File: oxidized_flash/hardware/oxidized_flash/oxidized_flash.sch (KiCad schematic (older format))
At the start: 37 parts, among them J1 USB_A, J2 Conn_ARM_JTAG_SWD_10, U1 LM1117-3.3, U2 ATSAMD51G18A-MU, U3 IS21ES

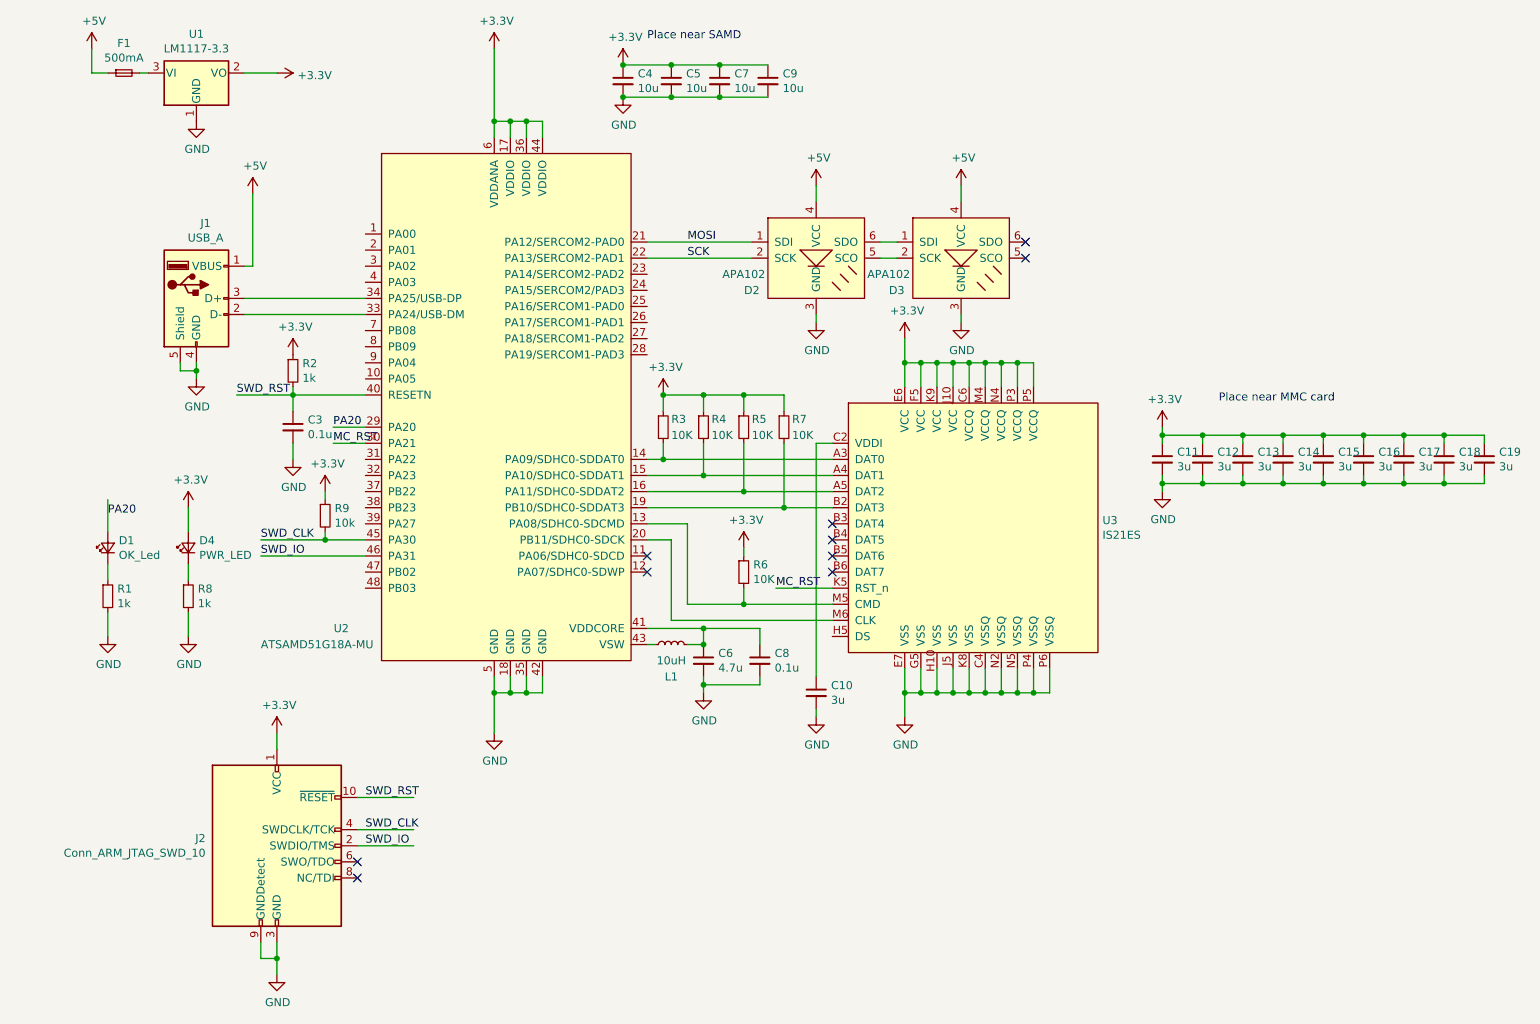
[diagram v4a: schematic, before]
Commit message: Rip out all the emmc stuff, just a samd with lights
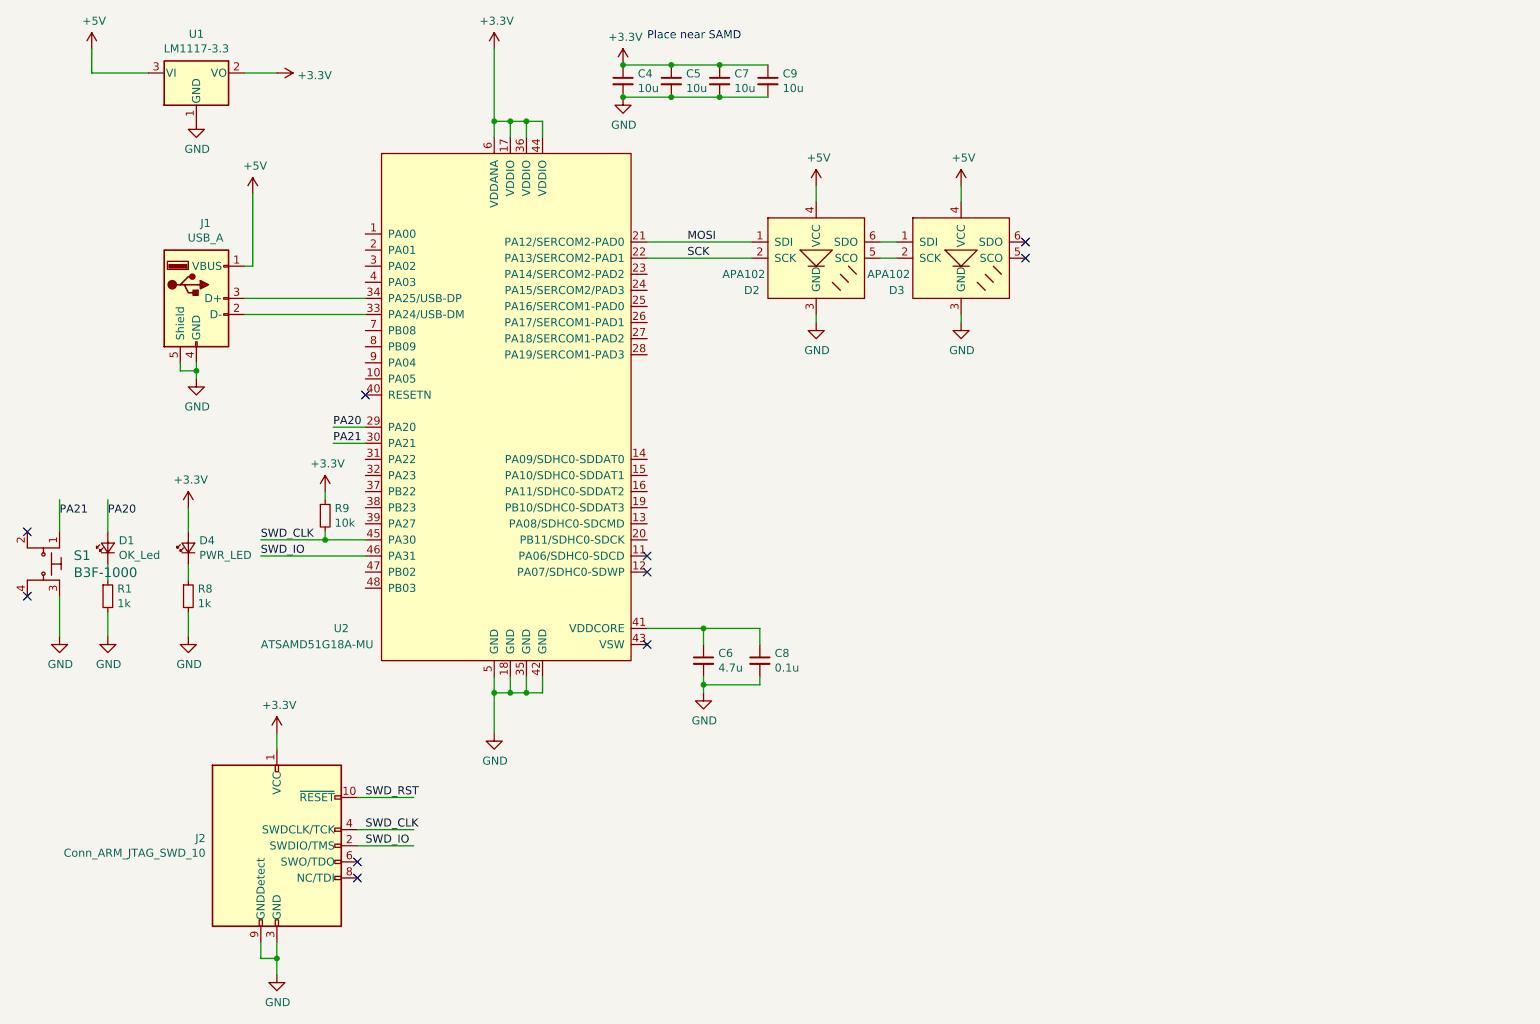
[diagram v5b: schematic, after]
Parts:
- removed C10, C11: 3u, Capacitor_SMD:C_0603_1608Metric, symbol Device:C_Small
- removed C12, C13, C14, C15, C16, C17, C18, C19: 3u, Capacitor_SMD:C_0603_1608Metric_Pad1.05x0.95mm_HandSolder, symbol Device:C_Small
- removed C3: 0.1u, Capacitor_SMD:C_0603_1608Metric, symbol Device:C_Small
- removed F1: 500mA, Fuse:Fuse_0603_1608Metric, symbol Device:Fuse_Small
- removed L1: 10uH, Inductor_SMD:L_0603_1608Metric, symbol Device:L_Small
- removed R2: 1k, Resistor_SMD:R_0603_1608Metric, symbol Device:R_Small
- removed R3, R4, R5: 10K, Resistor_SMD:R_0603_1608Metric, symbol Device:R_Small
- removed R6, R7: 10K, Resistor_SMD:R_0603_1608Metric_Pad1.05x0.95mm_HandSolder, symbol Device:R_Small
- removed U3: IS21ES, Custom_BGA:FBGA-153_14x14_11.5x13.0mm, symbol oxidized_flash-rescue:IS21ES-eMMC
- added S1: B3F-1000, Buttons_Switches_THT:SW_TH_Tactile_Omron_B3F-10xx, symbol dk_Tactile-Switches:B3F-1000
- C4, C5, C6, C7, C8, C9: footprint Capacitor_SMD:C_0603_1608Metric -> Capacitors_SMD:C_0603
- D1, D4: footprint LED_SMD:LED_0603_1608Metric -> LEDs:LED_0603
- J2: footprint Connector_PinHeader_1.27mm:PinHeader_2x05_P1.27mm_Vertical_SMD -> Pin_Headers:Pin_Header_Straight_2x05_Pitch1.27mm_SMD
- R1: footprint Resistor_SMD:R_0603_1608Metric -> Resistors_SMD:R_0603
- R8, R9: footprint Resistor_SMD:R_0603_1608Metric_Pad1.05x0.95mm_HandSolder -> Resistors_SMD:R_0603
- U1: footprint Package_TO_SOT_SMD:SOT-223 -> TO_SOT_Packages_SMD:SOT-223
- U2: footprint Package_DFN_QFN:QFN-48-1EP_7x7mm_P0.5mm_EP5.3x5.3mm -> Housings_DFN_QFN:QFN-48-1EP_7x7mm_Pitch0.5mm
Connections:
- net labels added: PA21
- net labels removed: MC_RST
- wire segments 184 -> 72
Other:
- note removed: "Place near MMC card"

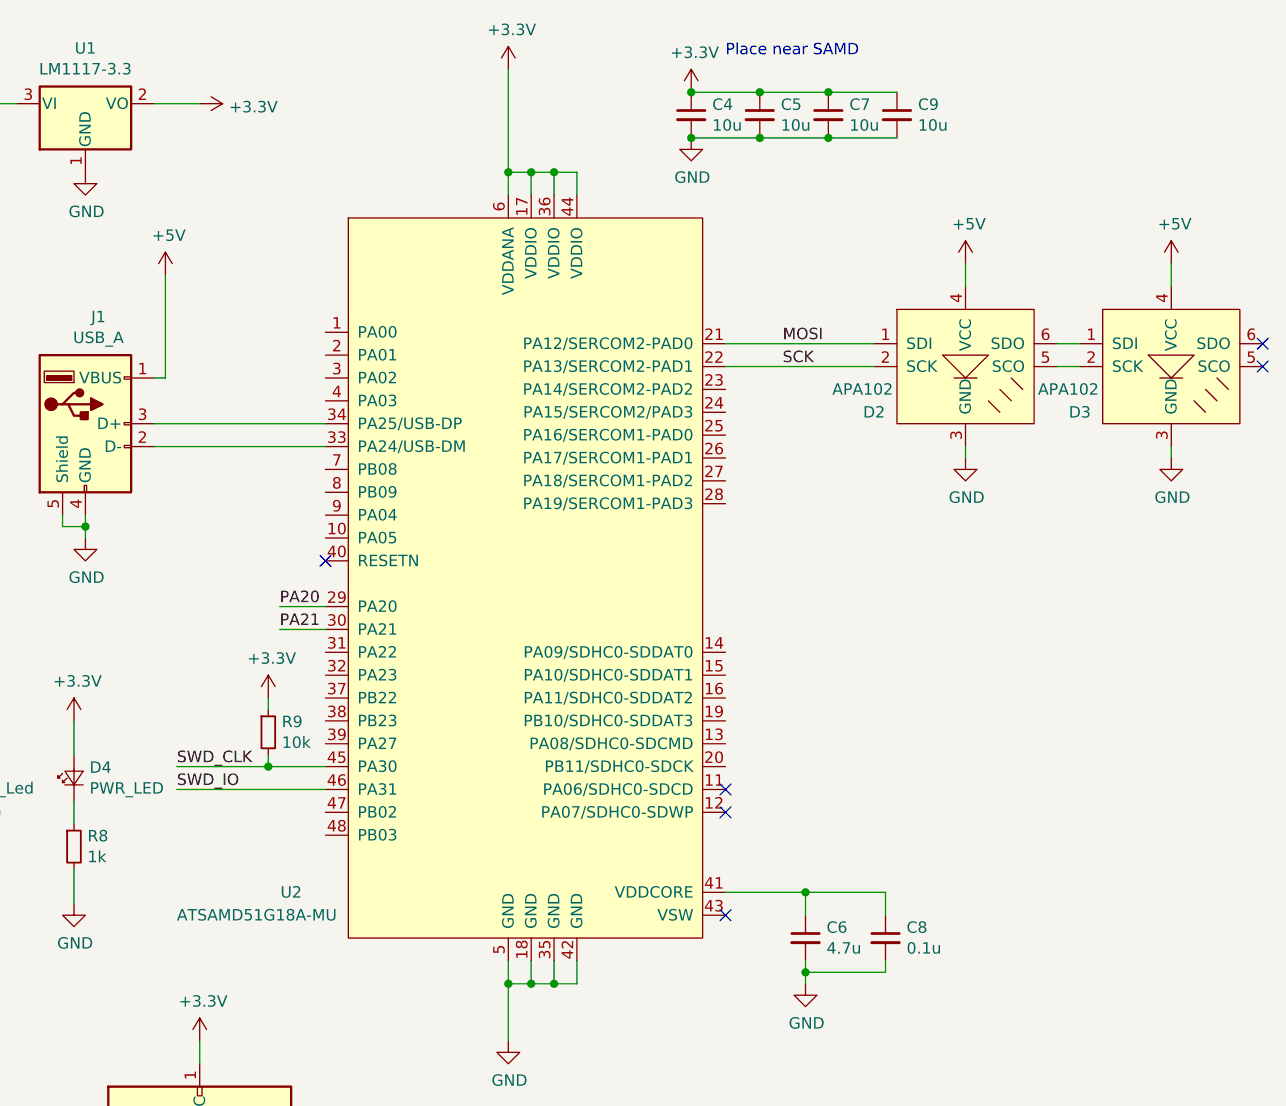
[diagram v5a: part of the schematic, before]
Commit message: Add 512M SPI flash
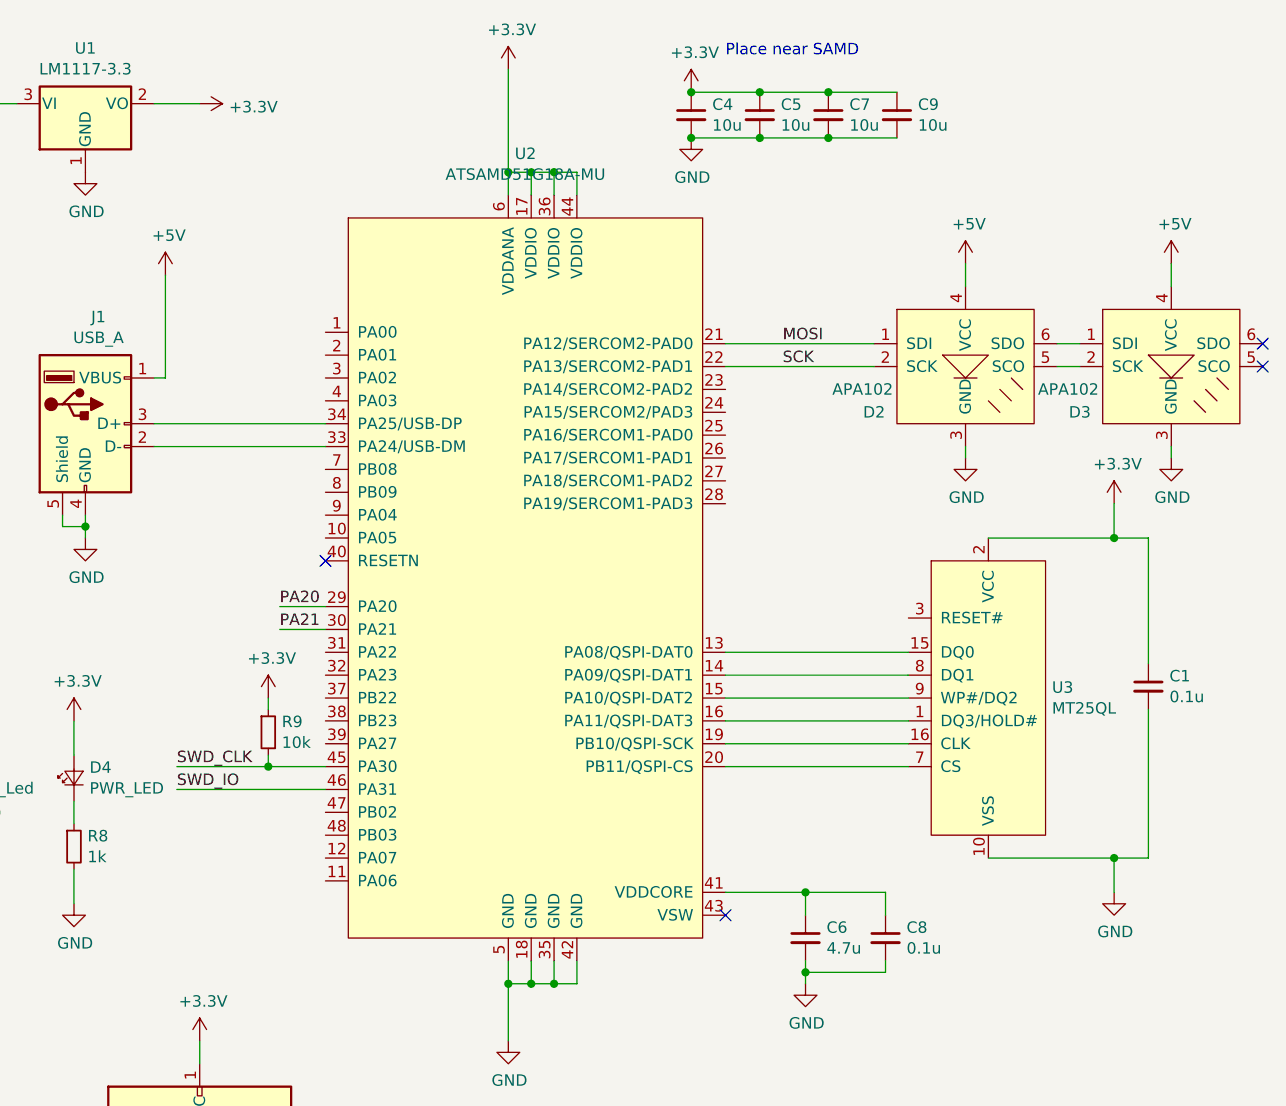
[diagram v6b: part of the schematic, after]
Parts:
- removed U2: ATSAMD51G18A-MU, Housings_DFN_QFN:QFN-48-1EP_7x7mm_Pitch0.5mm, symbol oxidized_flash-rescue:ATSAMD51G18A-MU-ATSAMD
- added C1: 0.1u, Capacitors_SMD:C_0603, symbol Device:C_Small
- added U2: ATSAMD51G18A-MU, Housings_DFN_QFN:QFN-48-1EP_7x7mm_Pitch0.5mm, symbol ATSAMD:ATSAMD51G18A-MU
- added U3: MT25QL, Housings_SSOP:SOP-16_4.4x10.4mm_Pitch1.27mm, symbol custom_ic:MT25QL
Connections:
- wire segments 72 -> 86
- no-connect marks 10 -> 8
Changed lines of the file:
@@
 	1    0    0    -1
 $EndComp
-NoConn ~ 4400 4200
-NoConn ~ 4400 4300
 Wire Wire Line
 	3450 4950 3450 5050
@@
 Wire Wire Line
 	3450 1600 3450 1500
-Wire Wire Line
-	1900 2600 2650 2600
-Wire Wire Line
-	1900 2700 2650 2700
 Wire Wire Line
 	3550 1600 3550 1500
@@
 PA20
 Wire Wire Line
-	2450 3400 2650 3400
-Wire Wire Line
 	1900 1200 2100 1200
 Wire Wire Line
@@
 Connection ~ 2400 4100
 Wire Wire Line
-	2400 4100 2650 4100
-Wire Wire Line
 	2400 3850 2400 3800
 $Comp
@@
 	1    0    0    -1
 $EndComp
-Wire Wire Line
-	2650 4200 2000 4200
 Text Label 2000 4200 0    50   ~ 0
 SWD_IO
@@
 Text Label 2450 3500 0    50   ~ 0
 PA21
-Wire Wire Line
-	2650 3500 2450 3500
 Wire Wire Line
 	750  3850 750  4050
@@
 Wire Wire Line
 	3450 5050 3450 5300
-$Comp
-L oxidized_flash-rescue:ATSAMD51G18A-MU-ATSAMD U2
-U 1 1 5C4804F6
+NoConn ~ 2650 3200
+$Comp
+L ATSAMD:ATSAMD51G18A-MU U2
+U 1 1 5E0421D4
 P 3600 3350
-F 0 "U2" H 2500 2050 50  0000 C CNN
-F 1 "ATSAMD51G18A-MU" H 2350 1950 50  0000 C CNN
+F 0 "U2" H 3525 5281 50  0000 C CNN
+F 1 "ATSAMD51G18A-MU" H 3525 5190 50  0000 C CNN
 F 2 "Housings_DFN_QFN:QFN-48-1EP_7x7mm_Pitch0.5mm" H 3600 3350 50  0001 C CNN
 F 3 "" H 3600 3350 50  0001 C CNN
@@
 	1    0    0    -1
 $EndComp
-NoConn ~ 2650 3200
+$Comp
+L custom_ic:MT25QL U3
+U 1 1 5E04A147
+P 5500 3650
+F 0 "U3" H 5828 3546 50  0000 L CNN
+F 1 "MT25QL" H 5828 3455 50  0000 L CNN
+F 2 "Housings_SSOP:SOP-16_4.4x10.4mm_Pitch1.27mm" H 6450 3500 50  0001 C CNN
+F 3 "" H 6450 3500 50  0001 C CNN
+	1    5500 3650
+	1    0    0    -1
+$EndComp
+Wire Wire Line
+	4400 3600 5200 3600
+Wire Wire Line
+	1900 2600 2650 2600
+Wire Wire Line
+	1900 2700 2650 2700
+Wire Wire Line
+	2450 3400 2650 3400
+Wire Wire Line
+	2400 4100 2650 4100
+Wire Wire Line
+	2000 4200 2650 4200
+Wire Wire Line
+	2450 3500 2650 3500
+Wire Wire Line
+	4400 3700 5200 3700
+Wire Wire Line
+	4400 3800 5200 3800
+Wire Wire Line
+	4400 3900 5200 3900
+Wire Wire Line
+	4400 4000 5200 4000
+Wire Wire Line
+	4400 4100 5200 4100
+$Comp
+L Device:C_Small C1
+U 1 1 5E055AF7
+P 6250 3750
+F 0 "C1" H 6342 3796 50  0000 L CNN
+F 1 "0.1u" H 6342 3705 50  0000 L CNN
+F 2 "Capacitors_SMD:C_0603" H 6250 3750 50  0001 C CNN
+F 3 "~" H 6250 3750 50  0001 C CNN
+	1    6250 3750
+	1    0    0    -1
+$EndComp
+Wire Wire Line
+	5550 3100 6100 3100
+Wire Wire Line
+	6250 3100 6250 3650
+Wire Wire Line
+	6250 3850 6250 4500
+Wire Wire Line
+	6250 4500 6100 4500
+$Comp
+L power:+3.3V #PWR08
+U 1 1 5E05A40F
+P 6100 2950
+F 0 "#PWR08" H 6100 2800 50  0001 C CNN
+F 1 "+3.3V" H 6115 3123 50  0000 C CNN
+F 2 "" H 6100 2950 50  0001 C CNN
+F 3 "" H 6100 2950 50  0001 C CNN
+	1    6100 2950
+	1    0    0    -1
+$EndComp
+Wire Wire Line
+	6100 3100 6100 2950
+Connection ~ 6100 3100
+Wire Wire Line
+	6100 3100 6250 3100
+$Comp
+L power:GND #PWR09
+U 1 1 5E05E6A1
+P 6100 4650
+F 0 "#PWR09" H 6100 4400 50  0001 C CNN
+F 1 "GND" H 6105 4477 50  0000 C CNN
+F 2 "" H 6100 4650 50  0001 C CNN
+F 3 "" H 6100 4650 50  0001 C CNN
+	1    6100 4650
+	1    0    0    -1
+$EndComp
+Wire Wire Line
+	6100 4500 6100 4650
+Connection ~ 6100 4500
+Wire Wire Line
+	6100 4500 5550 4500
 $EndSCHEMATC

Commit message: Update APA and flash footprints
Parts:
- D2, D3: footprint Custom_LED:APA102-2020 -> Custom_LED:LED_RGB_5050-6
- U3: footprint Housings_SSOP:SOP-16_4.4x10.4mm_Pitch1.27mm -> Custom_IC:SOP2-16
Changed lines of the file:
@@
 F 0 "D2" H 5050 2150 50  0000 C CNN
 F 1 "APA102" H 5000 2250 50  0000 C CNN
-F 2 "Custom_LED:APA102-2020" H 5450 2350 50  0001 C CNN
+F 2 "Custom_LED:LED_RGB_5050-6" H 5450 2350 50  0001 C CNN
 F 3 "" H 5450 2350 50  0001 C CNN
 	1    5450 2350
@@
 F 0 "D3" H 5950 2150 50  0000 C CNN
 F 1 "APA102" H 5900 2250 50  0000 C CNN
-F 2 "Custom_LED:APA102-2020" H 6350 2350 50  0001 C CNN
+F 2 "Custom_LED:LED_RGB_5050-6" H 6350 2350 50  0001 C CNN
 F 3 "" H 6350 2350 50  0001 C CNN
 	1    6350 2350
@@
 F 0 "U3" H 5828 3546 50  0000 L CNN
 F 1 "MT25QL" H 5828 3455 50  0000 L CNN
-F 2 "Housings_SSOP:SOP-16_4.4x10.4mm_Pitch1.27mm" H 6450 3500 50  0001 C CNN
+F 2 "Custom_IC:SOP2-16" H 6450 3500 50  0001 C CNN
 F 3 "" H 6450 3500 50  0001 C CNN
 	1    5500 3650

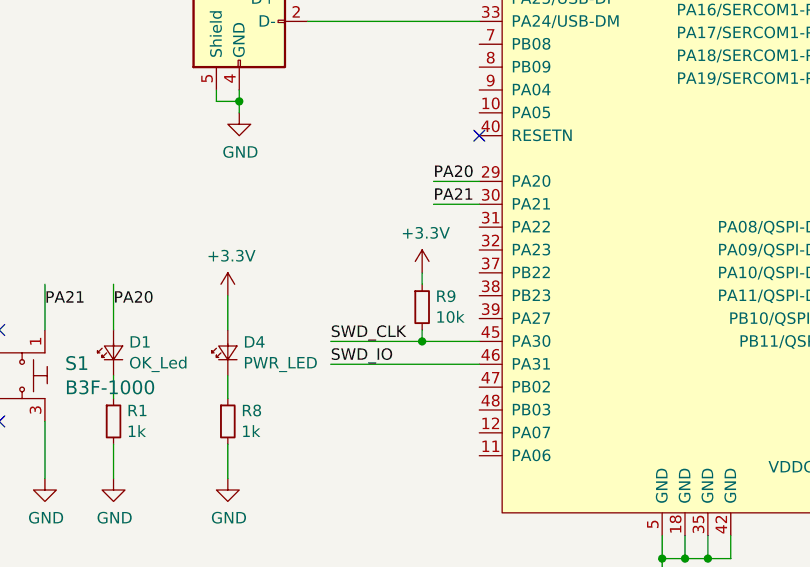
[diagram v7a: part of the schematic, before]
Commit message: Remove 10k pullup on SWD_IO
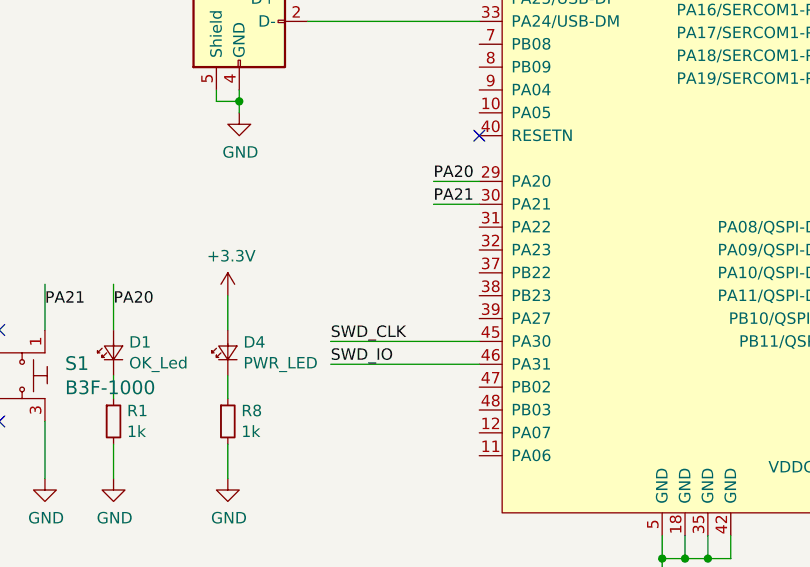
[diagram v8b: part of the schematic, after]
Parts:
- removed R9: 10k, Resistors_SMD:R_0603, symbol Device:R_Small
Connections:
- wire segments 86 -> 83
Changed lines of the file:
@@
 Text Label 2000 4100 0    50   ~ 0
 SWD_CLK
-$Comp
-L Device:R_Small R9
-U 1 1 5C752F56
-P 2400 3950
-F 0 "R9" H 2459 3996 50  0000 L CNN
-F 1 "10k" H 2459 3905 50  0000 L CNN
-F 2 "Resistors_SMD:R_0603" H 2400 3950 50  0001 C CNN
-F 3 "~" H 2400 3950 50  0001 C CNN
-	1    2400 3950
-	1    0    0    -1
-$EndComp
-Wire Wire Line
-	2000 4100 2400 4100
-Wire Wire Line
-	2400 4100 2400 4050
-Connection ~ 2400 4100
-Wire Wire Line
-	2400 3850 2400 3800
-$Comp
-L power:+3.3V #PWR0103
-U 1 1 5C770522
-P 2400 3800
-F 0 "#PWR0103" H 2400 3650 50  0001 C CNN
-F 1 "+3.3V" H 2415 3973 50  0000 C CNN
-F 2 "" H 2400 3800 50  0001 C CNN
-F 3 "" H 2400 3800 50  0001 C CNN
-	1    2400 3800
-	1    0    0    -1
-$EndComp
 Text Label 2000 4200 0    50   ~ 0
 SWD_IO
@@
 	2450 3400 2650 3400
 Wire Wire Line
-	2400 4100 2650 4100
-Wire Wire Line
 	2000 4200 2650 4200
 Wire Wire Line
@@
 Wire Wire Line
 	6100 4500 5550 4500
+Wire Wire Line
+	2000 4100 2650 4100
 $EndSCHEMATC
